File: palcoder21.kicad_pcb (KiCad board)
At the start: 2 copper layers, 43 x 63.5 mm, 27 parts, among them J1 Conn_01x10, J2 Conn_01x10, J3 Conn_01x01, J4 Conn_Coaxial, T1 2N2369, U1 82S129, U2 7474, U3 7404, U4 7407, Y1 8.86MHz

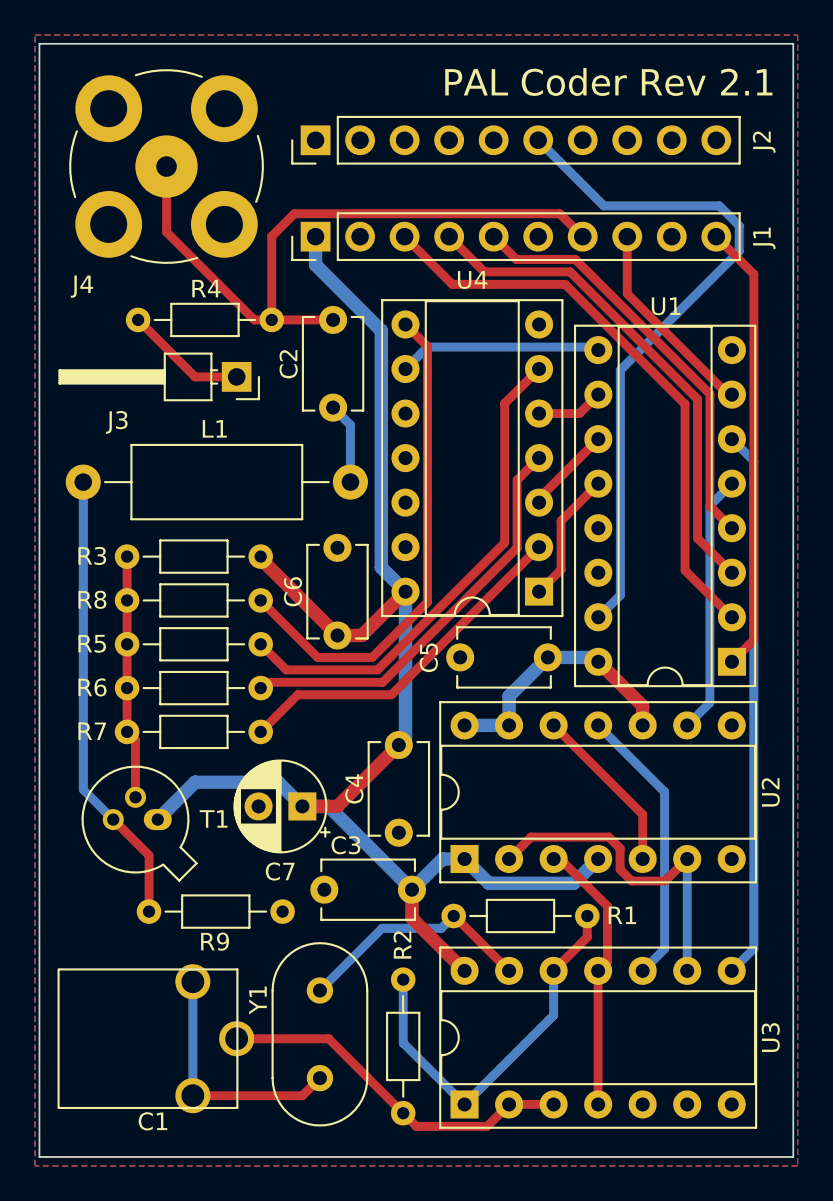
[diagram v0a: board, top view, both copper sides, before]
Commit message: Fix mistakes in first revision
Add missing trace

Fix swapped transistor pins

Use VCR instead of VNY
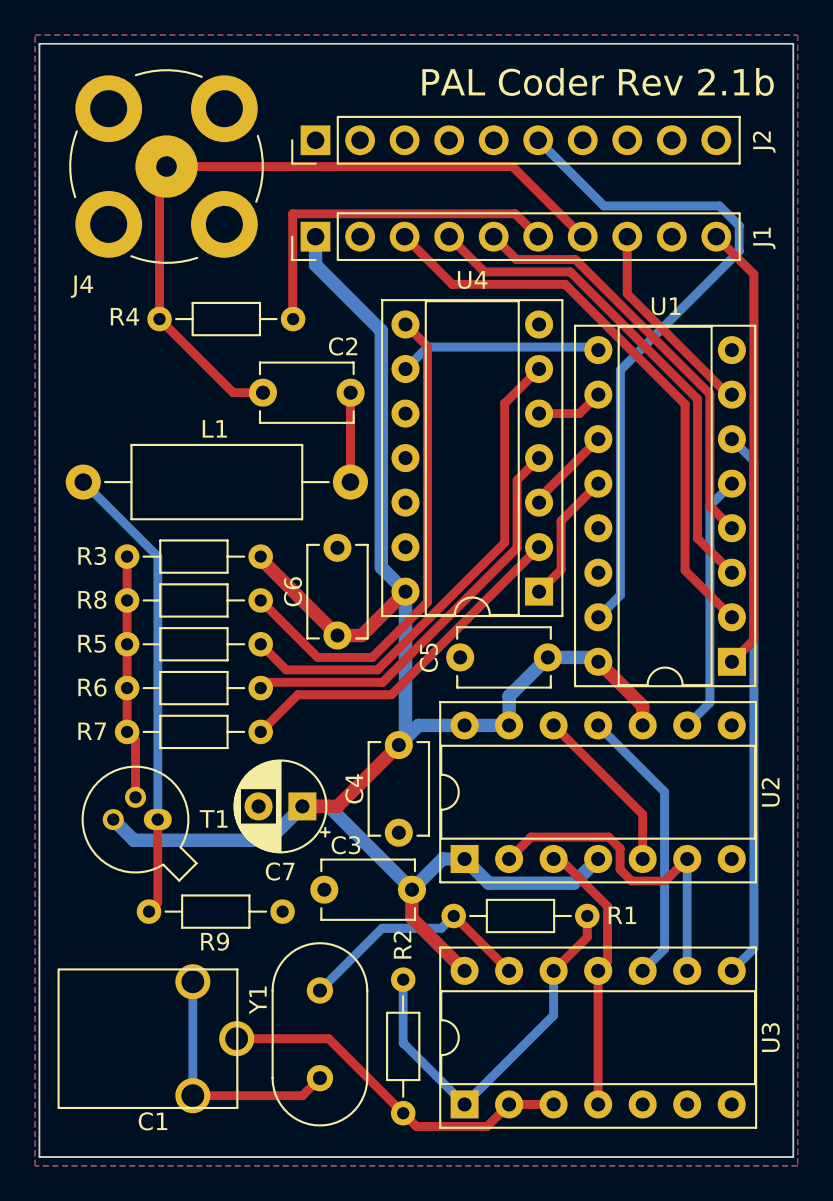
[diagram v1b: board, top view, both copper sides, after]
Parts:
- removed J3: Conn_01x01, Connector_PinHeader_2.54mm:PinHeader_1x01_P2.54mm_Horizontal
- C2: value 22 -> 120pF
- R4: value 560 -> 120
- moved R4 6.40 mm to (71.6, 90.2), turned to 0 degrees
- moved C2 1.31 mm to (82.5, 94.4), turned to 180 degrees
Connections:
- J1 pad 6: Net-(J1-Pad6) -> /VCR
- J1 pad 9: Net-(J1-Pad9) -> unconnected-(J1-Pad9)
- J2 pad 1: Net-(J2-Pad1) -> unconnected-(J2-Pad1)
- J2 pad 10: Net-(J2-Pad10) -> unconnected-(J2-Pad10)
- J2 pad 2: Net-(J2-Pad2) -> unconnected-(J2-Pad2)
- J2 pad 3: Net-(J2-Pad3) -> unconnected-(J2-Pad3)
- J2 pad 4: Net-(J2-Pad4) -> unconnected-(J2-Pad4)
- J2 pad 5: Net-(J2-Pad5) -> unconnected-(J2-Pad5)
- J2 pad 7: Net-(J2-Pad7) -> unconnected-(J2-Pad7)
- J2 pad 8: Net-(J2-Pad8) -> unconnected-(J2-Pad8)
- J2 pad 9: Net-(J2-Pad9) -> unconnected-(J2-Pad9)
- R4 pad 2: /VNY -> /VCR
- T1 pad 1: VCC -> Net-(L1-Pad1)
- T1 pad 3: Net-(L1-Pad1) -> VCC
- U2 pad 8: Net-(U2-Pad8) -> unconnected-(U2-Pad8)
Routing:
- net /VCR: track 0.00 -> 20.6 mm
- net /VNY: track 6.97 -> 0.00 mm
- net VCC: track 100.7 -> 107.3 mm
- net /PALVC: track 38.9 -> 41.9 mm
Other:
- board text added: "PAL Coder Rev 2.1b"
- board text removed: "PAL Coder Rev 2.1"
